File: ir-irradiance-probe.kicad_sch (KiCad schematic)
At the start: 57 parts, among them J1 USB-C_UJC-HP-3-SMT-TR, J2 SM04B-SRSS-TB-LF-SN, J3 PinHeader_1x2_P2.54mm_Drill1.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, J4 Conn_BNC_031-70526-21, SW1 MSS3-V-T_R, U1 TLV70033_SC70, U2 AD8604ARUZ, U3 ADC101C027CIMK

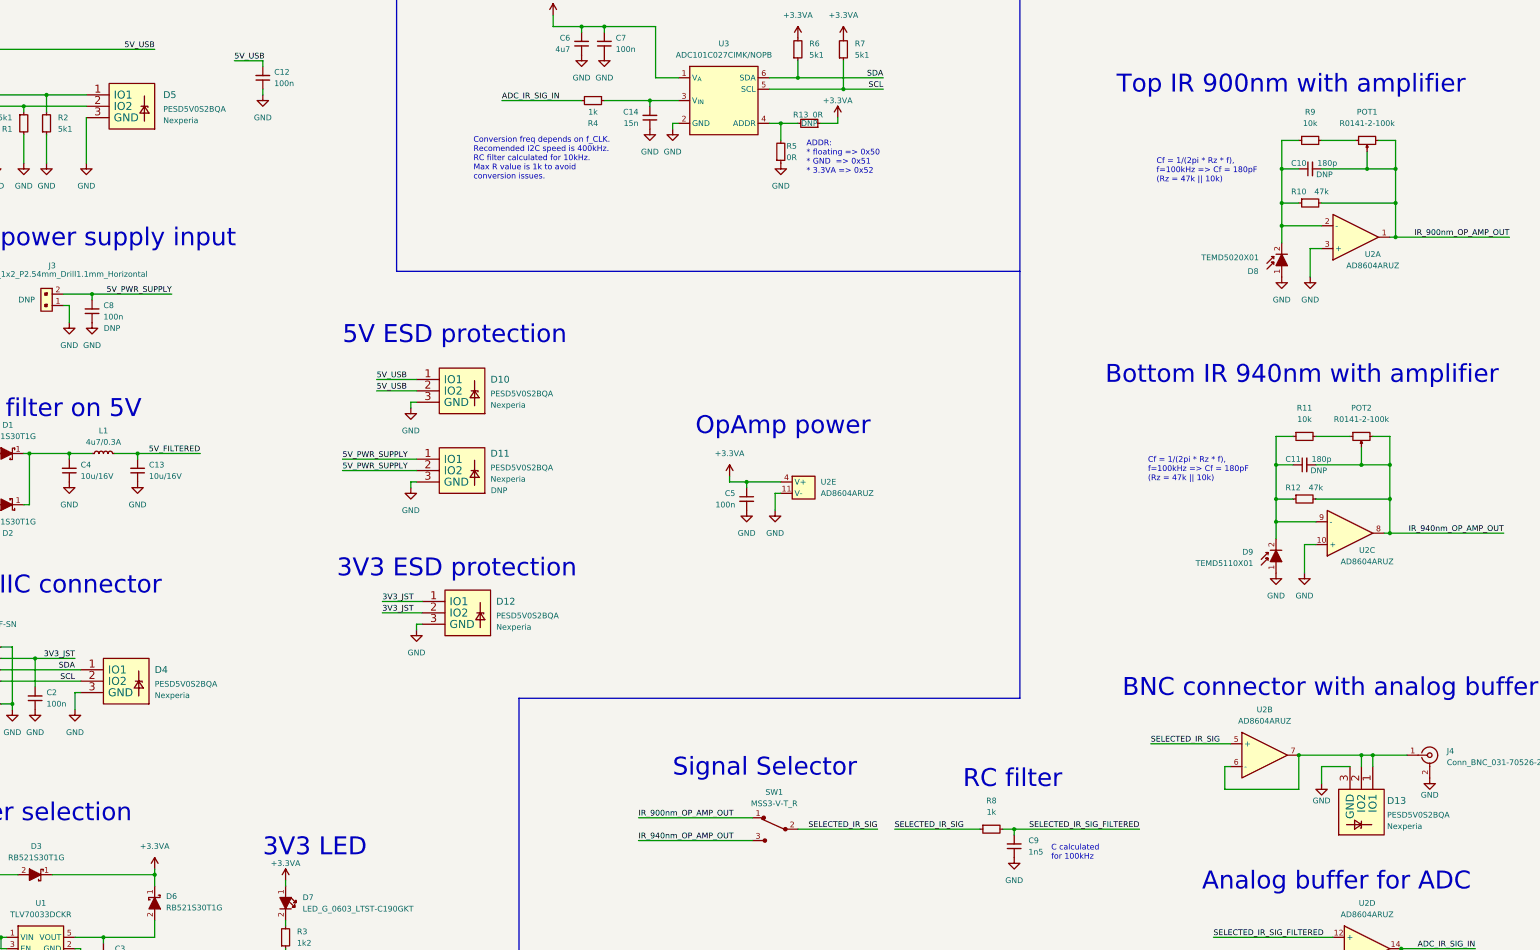
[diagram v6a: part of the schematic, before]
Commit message: [#47284] Standardized the rest of the components
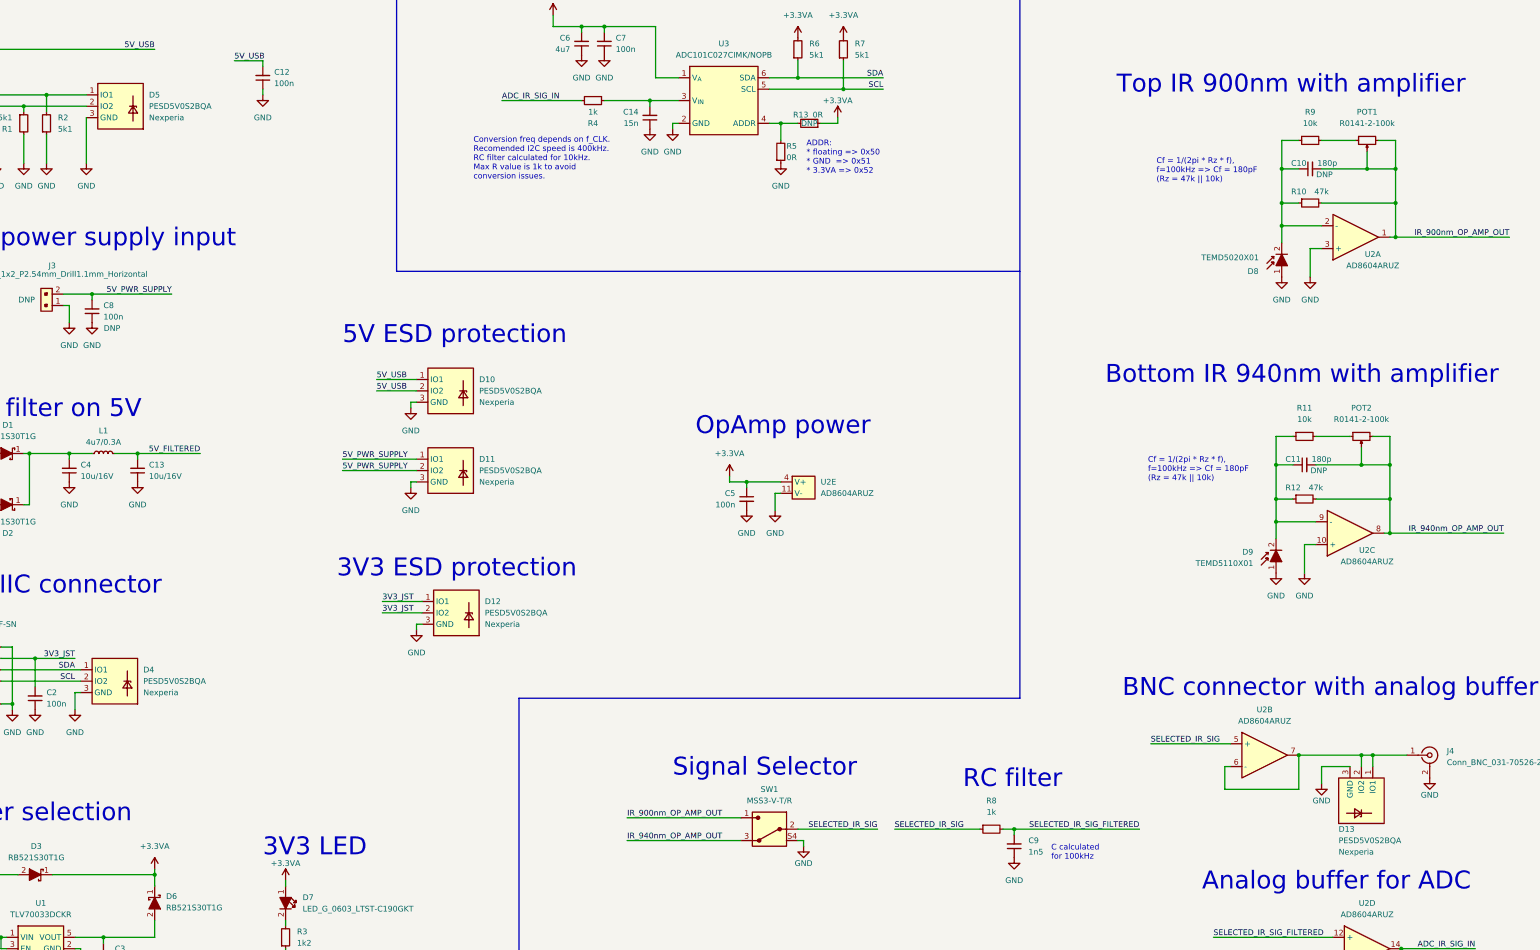
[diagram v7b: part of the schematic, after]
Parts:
- D10, D12, D13, D4, D5, SW1: Author (none) -> Antmicro; License (none) -> Apache-2.0
- D11: Author (none) -> Antmicro; DNP DNP -> (none); License (none) -> Apache-2.0
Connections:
- net GND: now also SW1.S1 (SH), SW1.S2 (SH), SW1.S3 (SH), SW1.S4 (SH)
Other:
- moved on the sheet: D10, D11, D12, D13, D4, D5

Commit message: [47284] Add preliminary routing
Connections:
- net IR_900nm_OP_AMP_OUT: now also SW1.3; no longer SW1.1
- net IR_940nm_OP_AMP_OUT: now also SW1.1; no longer SW1.3
